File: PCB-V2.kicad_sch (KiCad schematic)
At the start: 33 parts, among them J1 TB010-508-02BE, J2 TB010-508-02BE, J3 TB004-508-03BE, J4 TB004-508-03BE, U2 *, U3 6N137, U4 6N137, U5 *, U6 MC78M05CTG

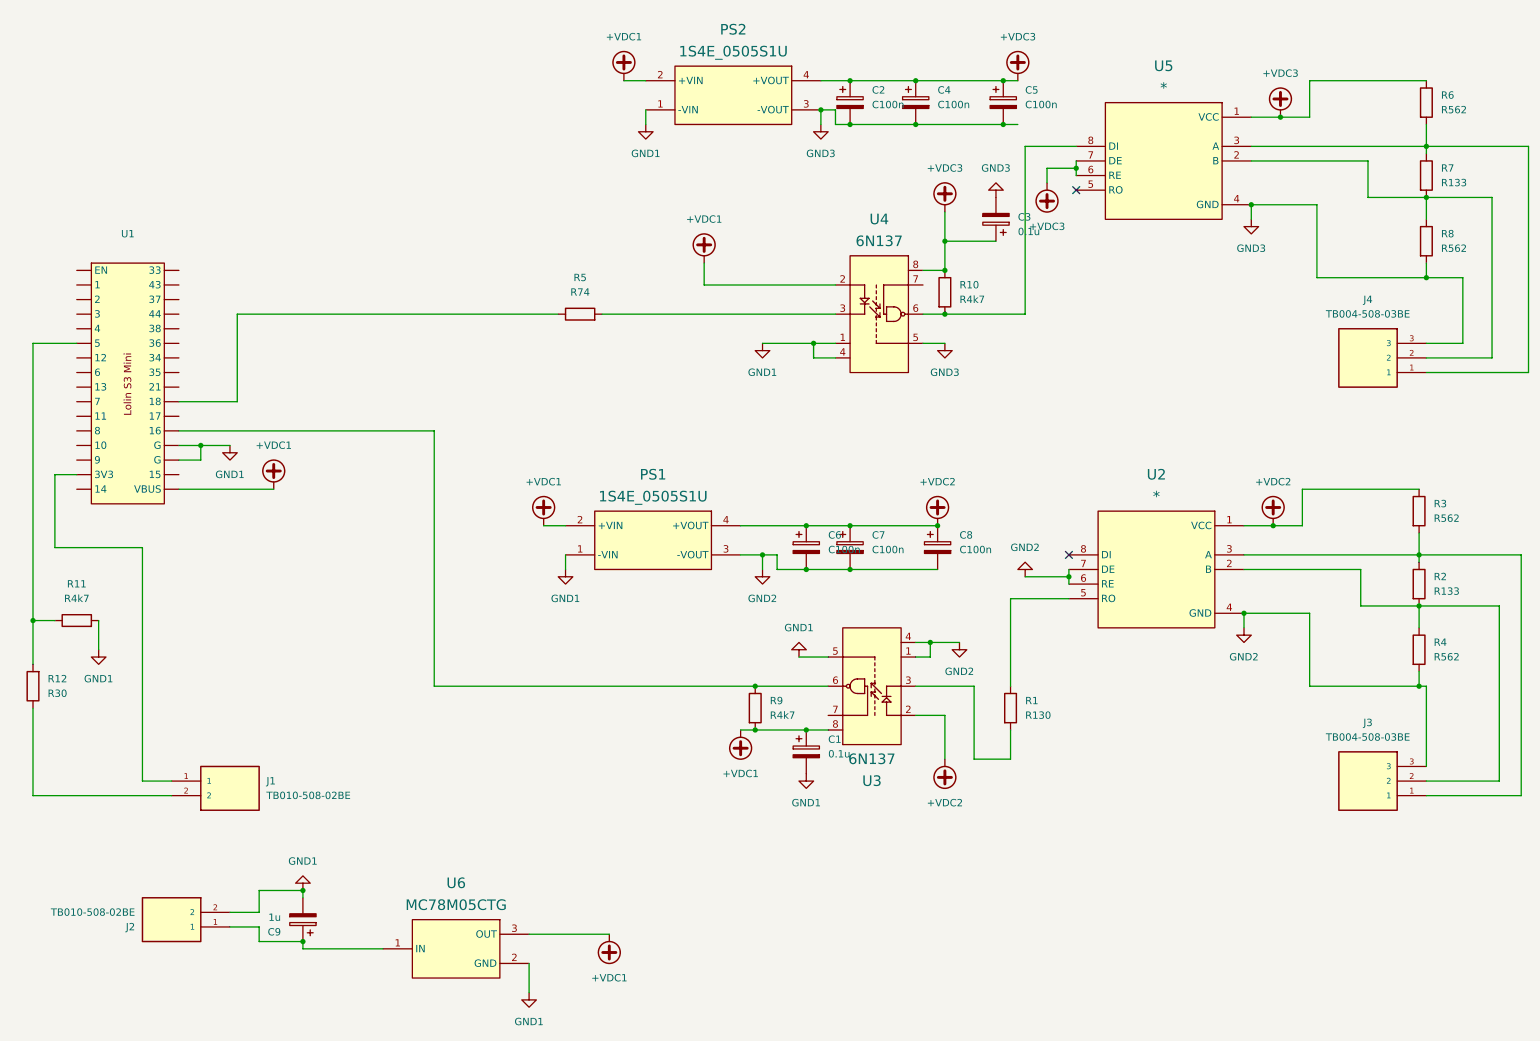
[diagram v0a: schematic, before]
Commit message: upgrade to more robust switch network
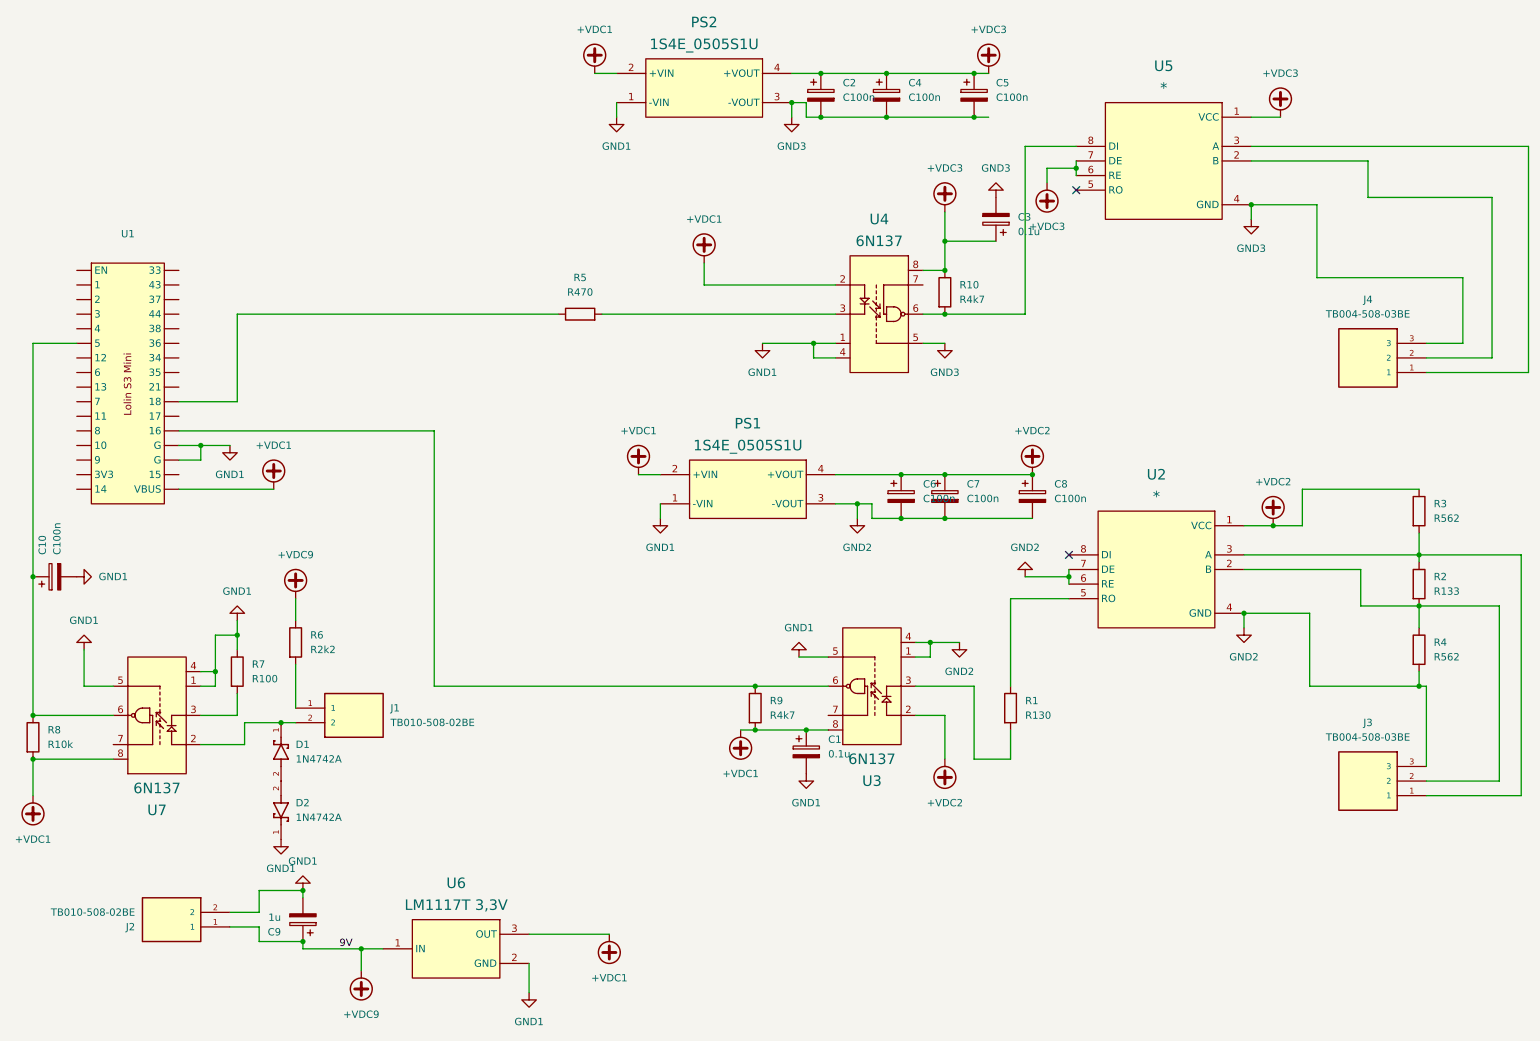
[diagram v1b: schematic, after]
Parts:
- removed R11: R4k7, dmx_interceptor:R_THT, symbol Device:R
- removed R12: R30, dmx_interceptor:R_THT, symbol Device:R
- added C10: C100n, Capacitor_THT:CP_Radial_D5.0mm_P2.50mm, symbol Device:C_Polarized
- added D1, D2: 1N4742A, dmx_interceptor:DIOAD1036W78L463D237, symbol dmx_interceptor:1N4742A
- added U7: 6N137, dmx_interceptor:DIP762W50P254L1016H465Q8, symbol dmx_interceptor:6N137
- R5: value R74 -> R470
- R6: value R562 -> R2k2
- R7: value R133 -> R100
- R8: value R562 -> R10k
- U6: value MC78M05CTG -> LM1117T 3,3V
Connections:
- net +VDC1: now also R8.2, U7.8 (VCC)
- net +VDC3: no longer R6.1
- net GND1: now also R7.1, C10.2, D2.1, U7.1 (NC), U7.4 (NC), U7.5 (GND)
- net GND3: no longer R8.2
- net at J4.2, U5.2 (B): no longer R7.2, R8.1
- net at J4.1, U5.3 (A): no longer R6.2, R7.1
- net +VDC9: now reaches C9.1, J2.1, U6.1 (IN)
- net +VDC9: now also R6.1
- net at J1.2: now also D1.1, U7.2 (A)
- net at U1.5: now also R8.1, C10.1, U7.6 (VO)
- net at J1.1: now also R6.2; no longer U1.3V3
- new net: R7.2, U7.3 (C)
- new net: D1.2, D2.2
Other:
- moved on the sheet: C2, C4, C5, C6, C7, C8, J1, PS1, PS2

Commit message: more robustness in switch pin
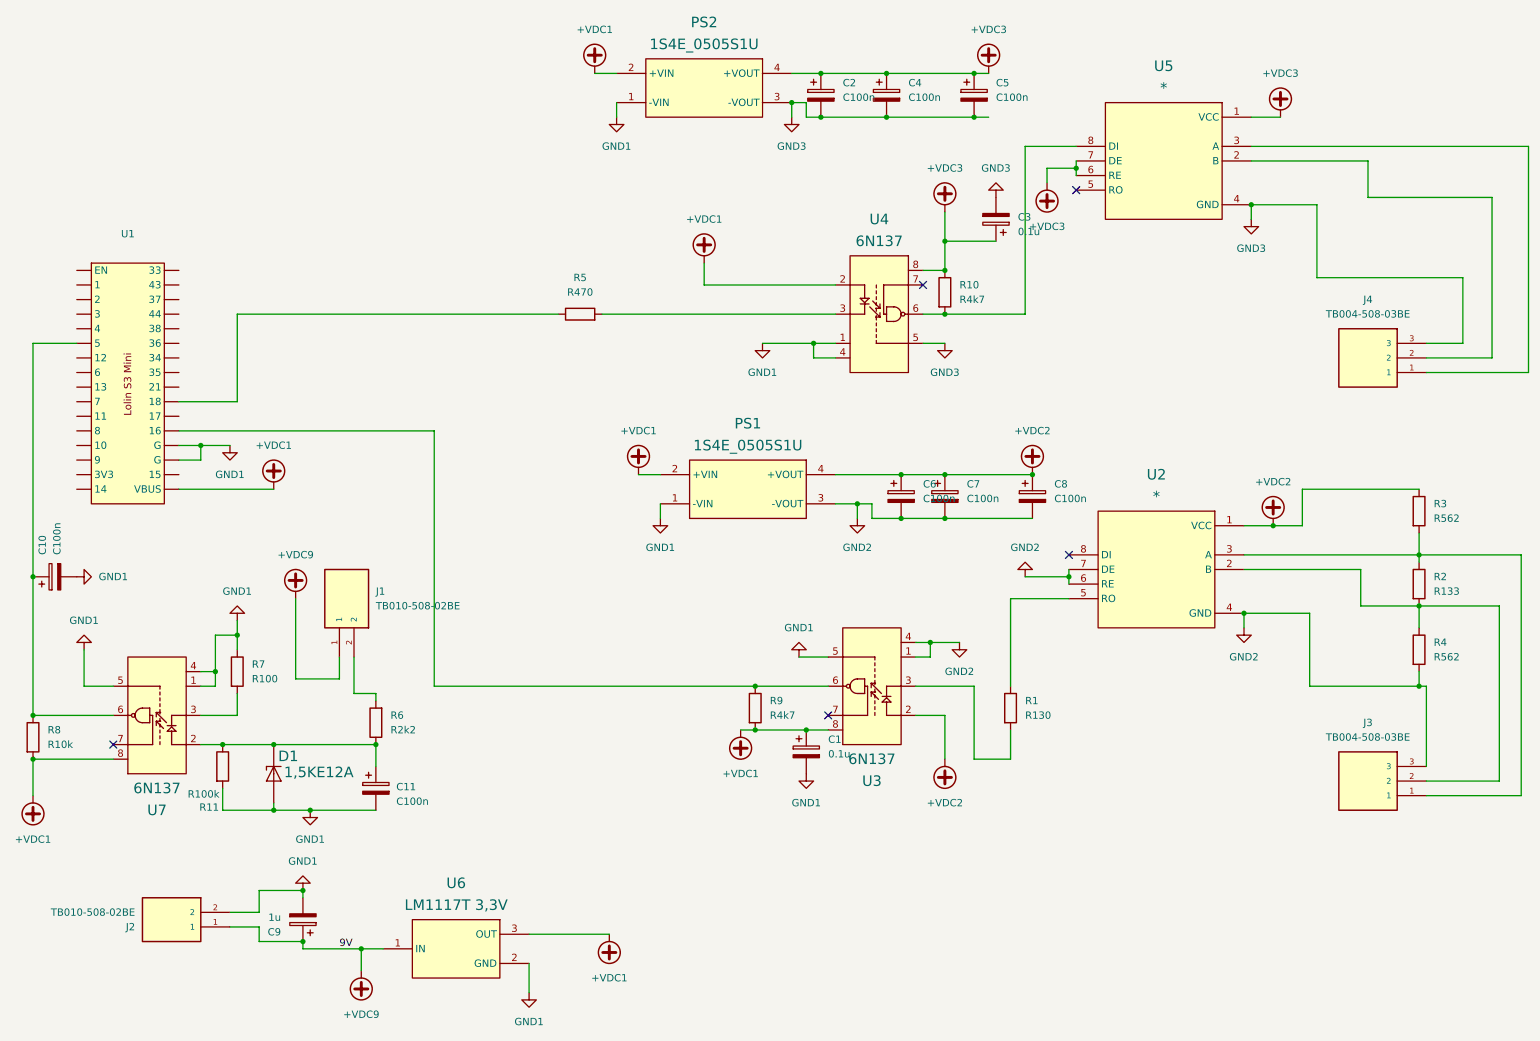
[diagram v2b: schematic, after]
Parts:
- removed D1, D2: 1N4742A, dmx_interceptor:DIOAD1036W78L463D237, symbol dmx_interceptor:1N4742A
- added C11: C100n, Capacitor_THT:CP_Radial_D5.0mm_P2.50mm, symbol Device:C_Polarized
- added D1: 1,5KE12A, dmx_interceptor:DIOAD1586W101L900D530, symbol dmx_interceptor:1.5KE12A
- added R11: R100k, dmx_interceptor:R_THT, symbol Device:R
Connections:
- net +VDC9: now also J1.1; no longer R6.1
- net GND1: now also C11.2, D1.A, R11.2
- net at R6.2: now also J1.2; no longer J1.1
- net at U7.2 (A): now also R6.1, C11.1, D1.C, R11.1; no longer J1.2
- no-connect marks 2 -> 5
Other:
- moved on the sheet: J1, R6
